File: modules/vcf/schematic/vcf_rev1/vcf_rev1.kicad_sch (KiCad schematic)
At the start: 15 parts, among them Q1 2N2978, Q2 BC548, Q3 BC548, U1 OP275

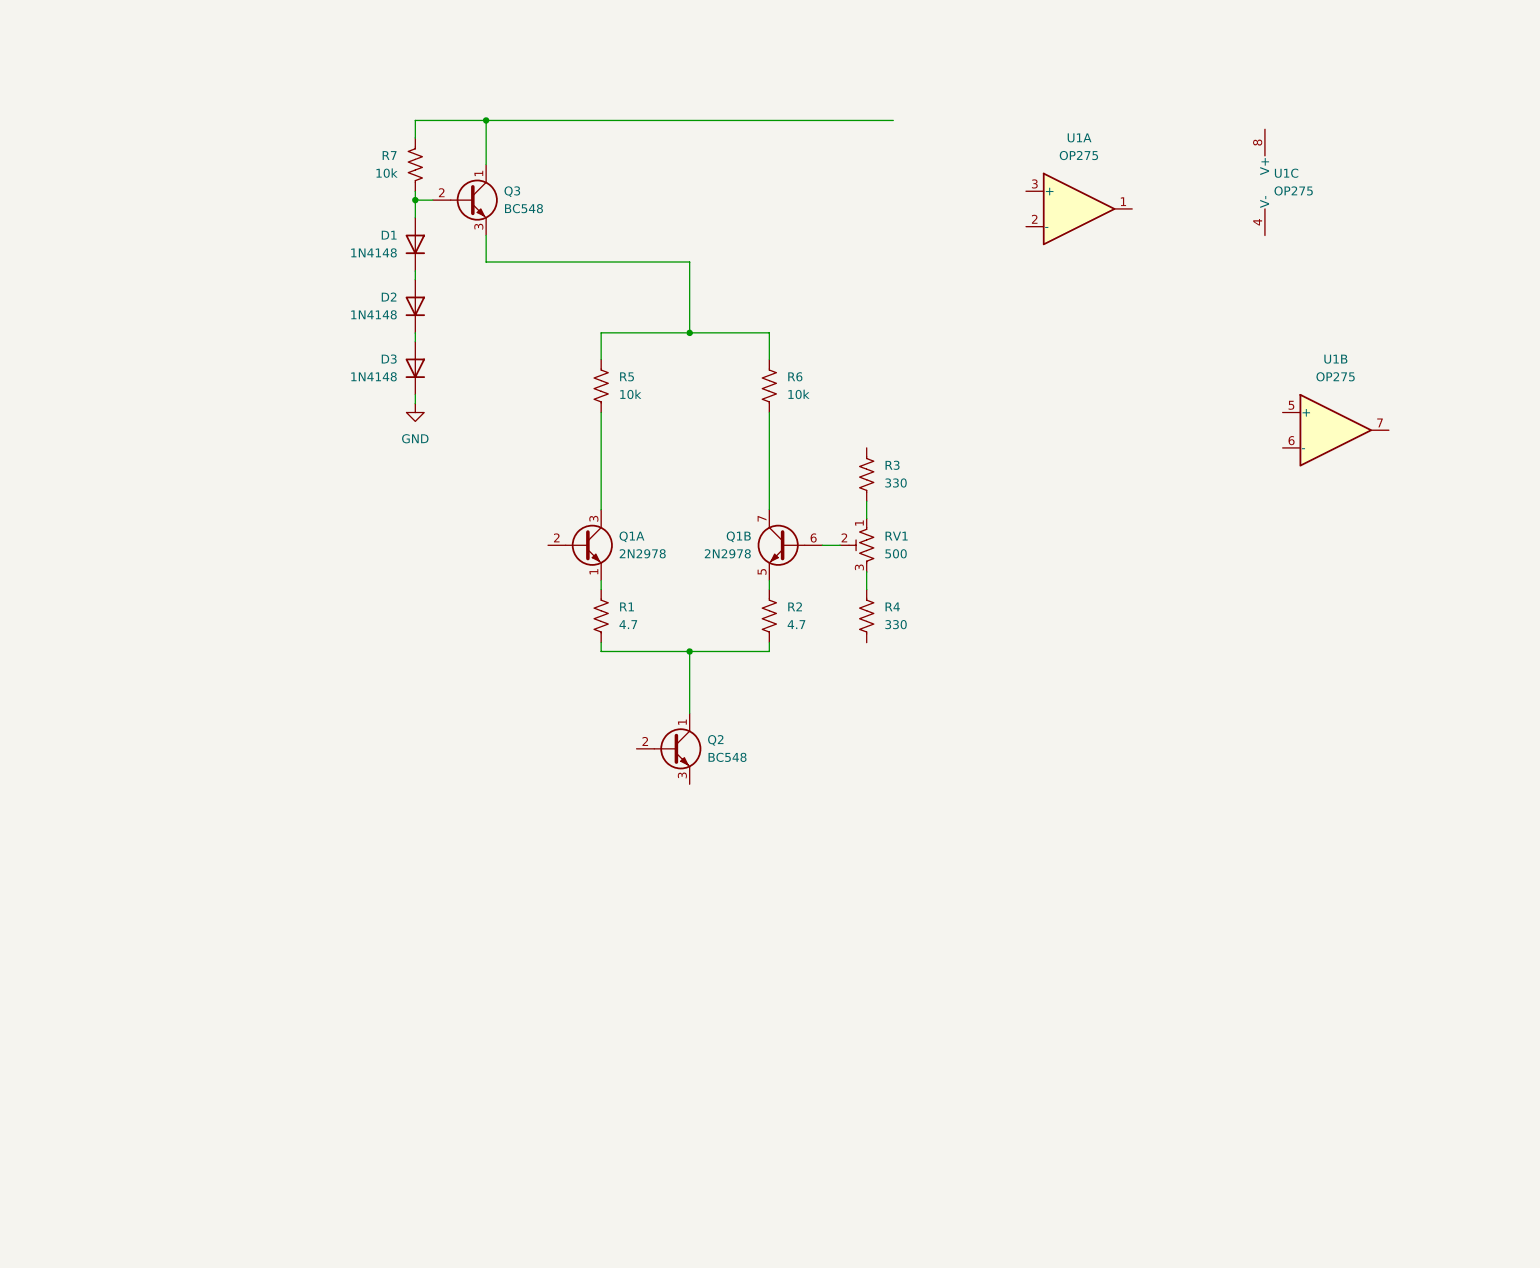
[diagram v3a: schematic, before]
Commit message: updated schematic for the headphones amp and VCF
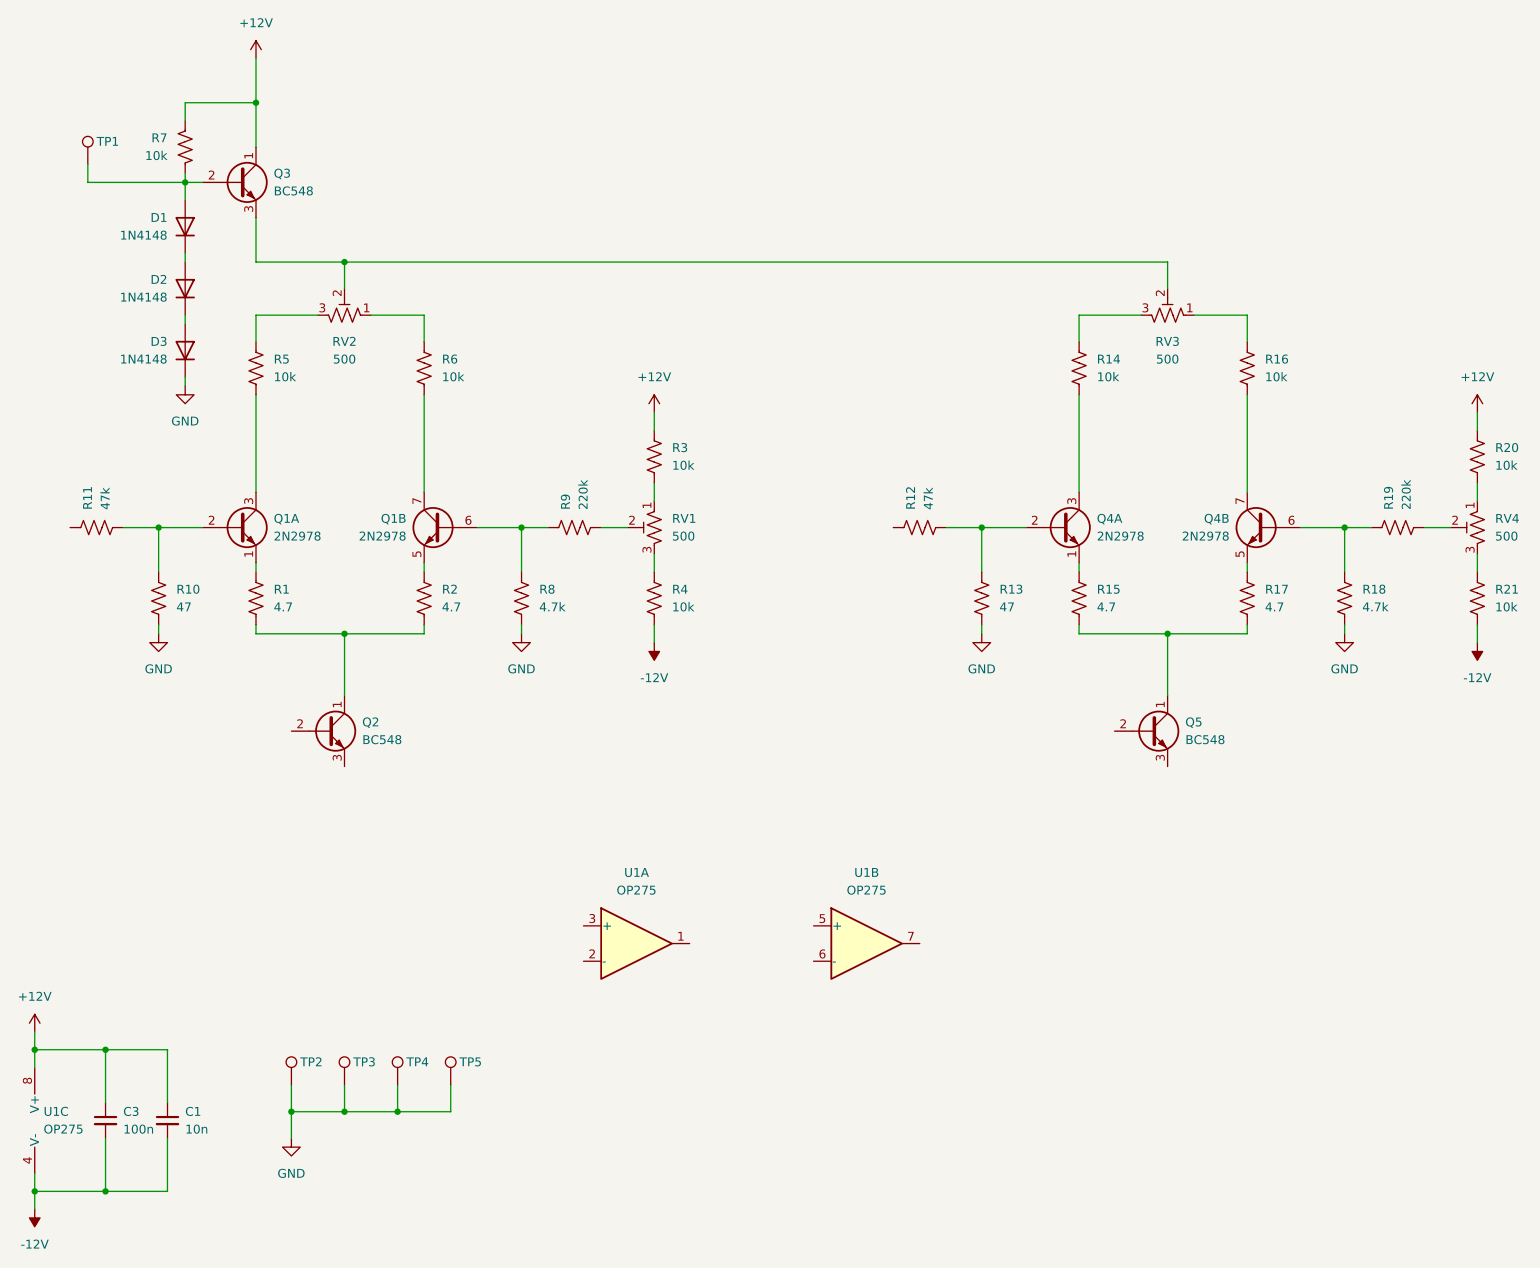
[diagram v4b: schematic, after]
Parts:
- added C1: 10n, Capacitor_THT:C_Rect_L7.0mm_W2.0mm_P5.00mm, symbol Device:C_Small
- added C3: 100n, Capacitor_THT:C_Rect_L7.0mm_W2.0mm_P5.00mm, symbol Device:C_Small
- added Q4: 2N2978, ProjectLib_Transient:TO-5-6, symbol ProjectLib_Transient:2N2978
- added Q5: BC548, Package_TO_SOT_THT:TO-92_Inline, symbol Transistor_BJT:BC548
- added R10, R13: 47, Resistor_THT:R_Axial_DIN0207_L6.3mm_D2.5mm_P10.16mm_Horizontal, symbol Device:R_US
- added R11, R12: 47k, Resistor_THT:R_Axial_DIN0207_L6.3mm_D2.5mm_P10.16mm_Horizontal, symbol Device:R_US
- added R14, R16, R20, R21: 10k, Resistor_THT:R_Axial_DIN0207_L6.3mm_D2.5mm_P10.16mm_Horizontal, symbol Device:R_US
- added R15, R17: 4.7, Resistor_THT:R_Axial_DIN0207_L6.3mm_D2.5mm_P10.16mm_Horizontal, symbol Device:R_US
- added R18, R8: 4.7k, Resistor_THT:R_Axial_DIN0207_L6.3mm_D2.5mm_P10.16mm_Horizontal, symbol Device:R_US
- added R19, R9: 220k, Resistor_THT:R_Axial_DIN0207_L6.3mm_D2.5mm_P10.16mm_Horizontal, symbol Device:R_US
- added RV2, RV3, RV4: 500, Potentiometer_THT:Potentiometer_Bourns_3296W_Vertical, symbol Device:R_Potentiometer_Trim_US
- added TP1, TP2, TP3, TP4, TP5: TestPoint, TestPoint:TestPoint_Pad_D2.0mm, symbol Connector:TestPoint
- R3, R4: value 330 -> 10k
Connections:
- net GND: now also R10.2, R13.2, R18.2, R8.2, TP2.1, TP3.1, TP4.1, TP5.1
- net -12V: now reaches U1.4 (V-)
- net -12V: now also R4.2, C1.2, C3.2, R21.2
- net +12V: now reaches U1.8 (V+)
- net +12V: now also Q3.1 (C), R3.1, R7.1, C1.1, C3.1, R20.1
- net at D1.2 (A), Q3.2 (B), R7.2: now also TP1.1
- net at Q1.6 (B2): now also R8.1, R9.1; no longer RV1.2
- net at Q1.2 (B1): now also R10.1, R11.2
- new net: Q4.5 (E2), R17.1
- new net: Q5.1 (C), R15.2, R17.2
- new net: Q4.6 (B2), R18.1, R19.1
- new net: Q4.7 (C2), R16.2
- new net: R5.1, RV2.3
- new net: R6.1, RV2.1
- new net: R20.2, RV4.1
- new net: R19.2, RV4.2
- new net: R21.1, RV4.3
- new net: Q4.1 (E1), R15.1
- new net: Q4.2 (B1), R12.2, R13.1
- new net: Q4.3 (C1), R14.2
- new net: R14.1, RV3.3
- new net: Q3.3 (E), RV2.2, RV3.2
- new net: R16.1, RV3.1
- new net: R9.2, RV1.2
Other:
- company: (none) -> QuBi
- title: (none) -> Voltage-Controlled Filter
- moved on the sheet: D1, D2, D3, Q1A, Q1B, Q2, Q3, R1, R2, R3, R4, R5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
